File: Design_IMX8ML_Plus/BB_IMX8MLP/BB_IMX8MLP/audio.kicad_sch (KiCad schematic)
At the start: 1 part, among them U30 NAU88C22YG

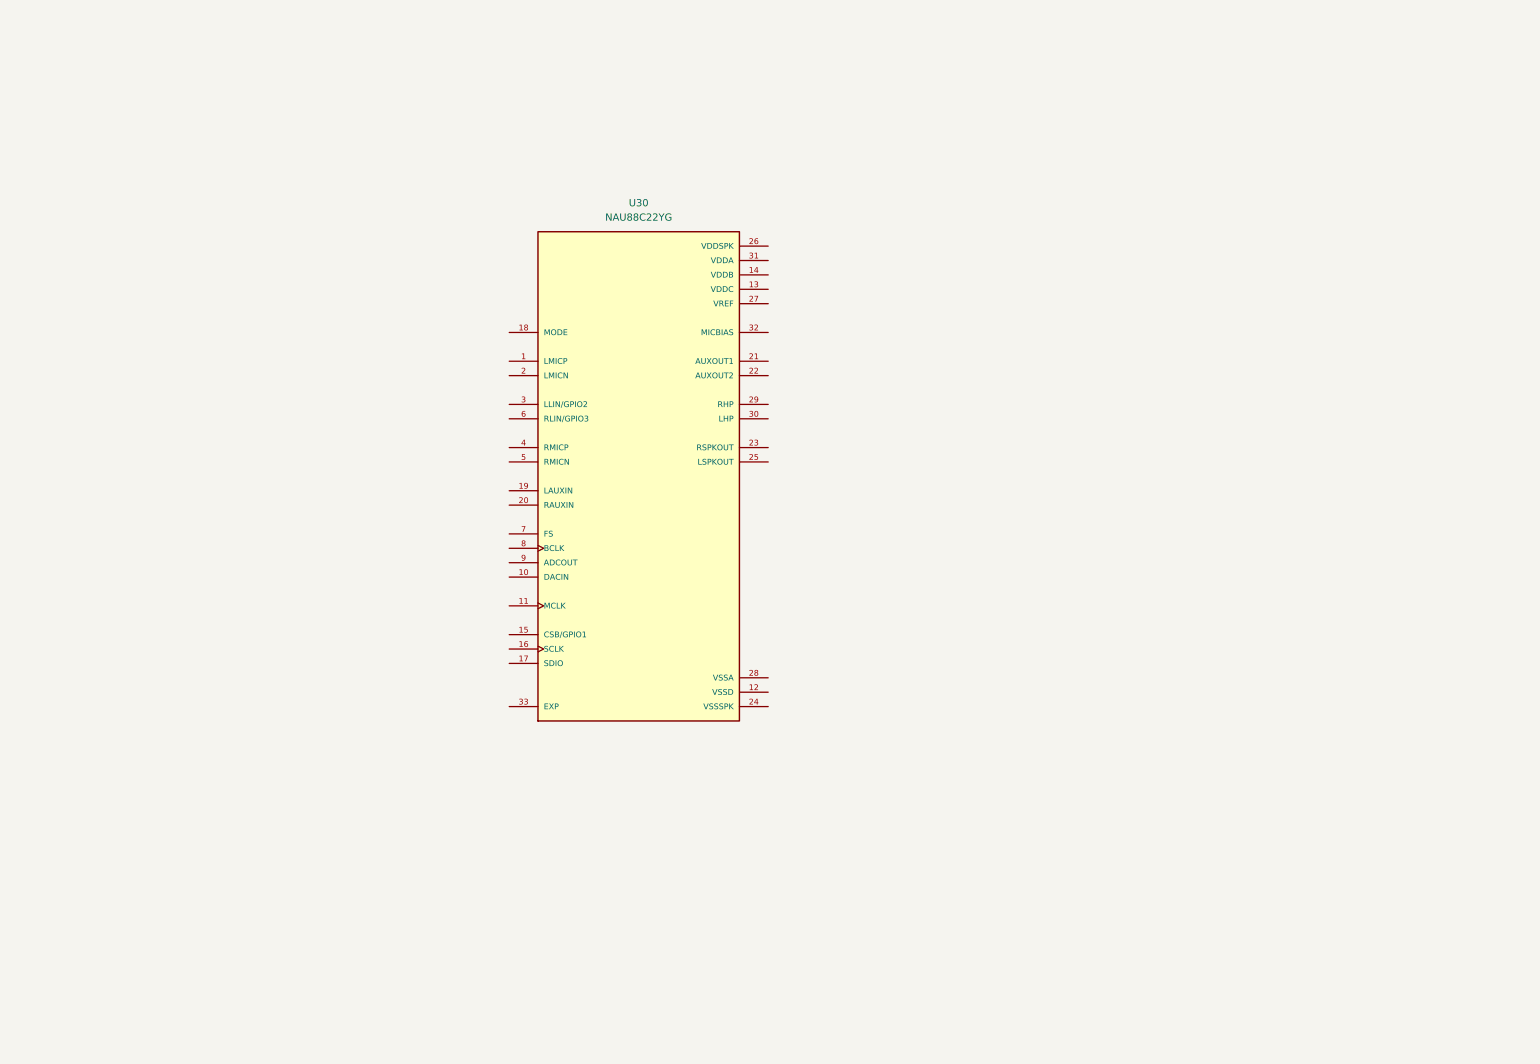
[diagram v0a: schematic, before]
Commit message: Adds audio interface
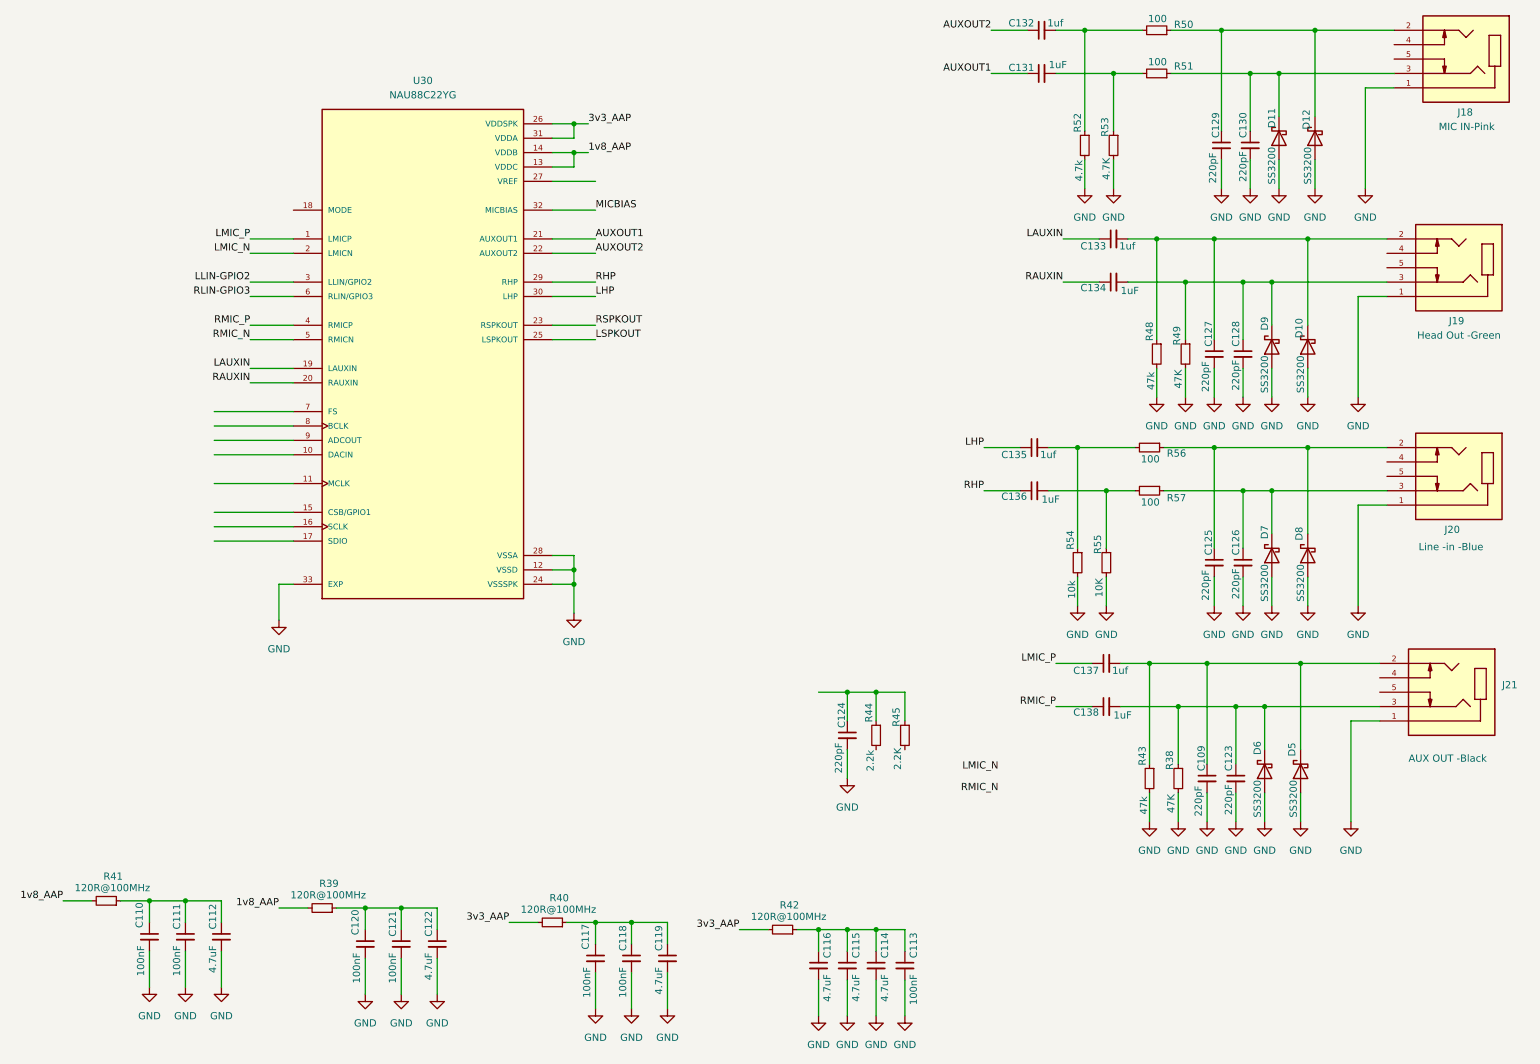
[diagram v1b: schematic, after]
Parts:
- added C109, C123, C124, C125, C126, C127, C128, C129, C130: 220pF, Capacitor_SMD:C_0402_1005Metric, symbol Device:C_Small
- added C110, C111, C113, C117, C118, C120, C121: 100nF, Capacitor_SMD:C_0402_1005Metric, symbol Device:C_Small
- added C112, C114, C115, C116, C119, C122: 4.7uF, Capacitor_SMD:C_0402_1005Metric, symbol Device:C_Small
- added C131, C134, C136, C138: 1uF, Capacitor_SMD:C_0402_1005Metric, symbol Device:C_Small
- added C132, C133, C135, C137: 1uf, Capacitor_SMD:C_0402_1005Metric, symbol Device:C_Small
- added D10, D11, D12, D5, D6, D7, D8, D9: SS3200, Diode_SMD:D_SMA, symbol Diode:SS3200
- added J18: MIC IN-Pink, _W_SBC:SJ1-3535NG-PI, symbol SJ1-3535NG-PI:SJ1-3535NG-PI
- added J19: Head Out -Green, _W_SBC:SJ1-3535NG-PI, symbol SJ1-3535NG-PI:SJ1-3535NG-PI
- added J20: Line -in -Blue, _W_SBC:SJ1-3535NG-PI, symbol SJ1-3535NG-PI:SJ1-3535NG-PI
- added J21: AUX OUT -Black, _W_SBC:SJ1-3535NG-PI, symbol SJ1-3535NG-PI:SJ1-3535NG-PI
- added R38, R49: 47K, Resistor_SMD:R_0402_1005Metric, symbol Device:R_Small
- added R39, R40, R41, R42: 120R@100MHz, Resistor_SMD:R_0402_1005Metric, symbol Device:R_Small
- added R43, R48: 47k, Resistor_SMD:R_0402_1005Metric, symbol Device:R_Small
- added R44: 2.2k, Resistor_SMD:R_0402_1005Metric, symbol Device:R_Small
- added R45: 2.2K, Resistor_SMD:R_0402_1005Metric, symbol Device:R_Small
- added R50, R51, R56, R57: 100, Resistor_SMD:R_0402_1005Metric, symbol Device:R_Small
- added R52: 4.7k, Resistor_SMD:R_0402_1005Metric, symbol Device:R_Small
- added R53: 4.7K, Resistor_SMD:R_0402_1005Metric, symbol Device:R_Small
- added R54: 10k, Resistor_SMD:R_0402_1005Metric, symbol Device:R_Small
- added R55: 10K, Resistor_SMD:R_0402_1005Metric, symbol Device:R_Small
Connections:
- net LMIC_P: now reaches U30.1 (LMICP)
- net LMIC_P: now also C137.1
- net GND: now reaches U30.12 (VSSD)
- net GND: now also U30.24 (VSSSPK), U30.28 (VSSA), U30.33 (EXP), C109.2, C110.2, C111.2, C112.2, C113.2, C114.2, C115.2, C116.2, C117.2, C118.2, C119.2, C120.2, C121.2, C122.2, C123.2, C124.2, C125.2, C126.2, C127.2, C128.2, C129.2, C130.2, D10.2 (A), D11.2 (A), D12.2 (A), D5.2 (A), D6.2 (A), D7.2 (A), D8.2 (A), D9.2 (A), J18.1, J19.1, J20.1, J21.1, R38.2, R43.2, R48.2, R49.2, R52.2, R53.2, R54.2, R55.2
- net 1v8_AAP: now reaches U30.13 (VDDC)
- net 1v8_AAP: now also U30.14 (VDDB), R39.2, R41.2
- net LAUXIN: now reaches U30.19 (LAUXIN)
- net LAUXIN: now also C133.1
- net LMIC_N: now reaches U30.2 (LMICN)
- net RAUXIN: now reaches U30.20 (RAUXIN)
- net RAUXIN: now also C134.1
- net AUXOUT1: now reaches U30.21 (AUXOUT1)
- net AUXOUT1: now also C131.1
- net AUXOUT2: now reaches U30.22 (AUXOUT2)
- net AUXOUT2: now also C132.1
- net RSPKOUT: now reaches U30.23 (RSPKOUT)
- net LSPKOUT: now reaches U30.25 (LSPKOUT)
- net 3v3_AAP: now reaches U30.26 (VDDSPK)
- net 3v3_AAP: now also U30.31 (VDDA), R40.2, R42.2
- net RHP: now reaches U30.29 (RHP)
- net RHP: now also C136.1
- net LLIN-GPIO2: now reaches U30.3 (LLIN/GPIO2)
- net LHP: now reaches U30.30 (LHP)
- net LHP: now also C135.1
- net MICBIAS: now reaches U30.32 (MICBIAS)
- net RMIC_P: now reaches U30.4 (RMICP)
- net RMIC_P: now also C138.1
- net RMIC_N: now reaches U30.5 (RMICN)
- net RLIN-GPIO3: now reaches U30.6 (RLIN/GPIO3)
- new net: C120.1, C121.1, C122.1, R39.1
- new net: C127.1, C133.2, D10.1 (K), J19.2, R48.1
- new net: C136.2, R55.1, R57.2
- new net: C135.2, R54.1, R56.2
- new net: C113.1, C114.1, C115.1, C116.1, R42.1
- new net: C126.1, D7.1 (K), J20.3, R57.1
- new net: C110.1, C111.1, C112.1, R41.1
- new net: C125.1, D8.1 (K), J20.2, R56.1
- new net: C129.1, D12.1 (K), J18.2, R50.1
- new net: C128.1, C134.2, D9.1 (K), J19.3, R49.1
- new net: C130.1, D11.1 (K), J18.3, R51.1
- new net: C109.1, C137.2, D5.1 (K), J21.2, R43.1
- new net: C131.2, R51.2, R53.1
- new net: C132.2, R50.2, R52.1
- new net: C123.1, C138.2, D6.1 (K), J21.3, R38.1
- new net: C117.1, C118.1, C119.1, R40.1
- new net: C124.1, R44.1, R45.1
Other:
- moved on the sheet: U30

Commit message: Review
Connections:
- net GND: now also U30.18 (MODE)
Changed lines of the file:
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@@
+	)
+	(junction
+		(at 62.23 114.3)
+		(diameter 0)
+		(color 0 0 0 0)
 	)
 	(junction
@@
 	(wire
 		(pts
+			(xy 62.23 48.26) (xy 64.77 48.26)
+		)
+		(stroke
+			(width 0)
+			(type default)
+		)
+	)
+	(wire
+		(pts
 			(xy 203.2 90.17) (xy 213.36 90.17)
 		)
@@
 		)
 		(stroke
+			(width 0)
+			(type default)
+		)
+	)
+	(wire
+		(pts
+			(xy 62.23 48.26) (xy 62.23 114.3)
+		)
+		(stroke

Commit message: pcb reorganization
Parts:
- removed D11, D12: SS3200, Diode_SMD:D_SMA, symbol Diode:SS3200
- added D13, D14: SS3200, Diode_SMD:D_SOD-923, symbol Diode:SS3200
- D10, D5, D6, D7, D8, D9: footprint Diode_SMD:D_SMA -> Diode_SMD:D_SOD-923
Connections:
- net GND: now also D13.2 (A), D14.2 (A)
- net at C127.1, C133.2, J19.2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: now also D14.1 (K); no longer D10.1 (K)
- net at C129.1, J18.2, R50.1: now also D10.1 (K)
- net at C128.1, C134.2, J19.3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: now also D13.1 (K); no longer D9.1 (K)
- net at C130.1, J18.3, R51.1: now also D9.1 (K)

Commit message: CPU Board actualizate
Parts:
- D10, D13, D14, D5, D6, D7, D8, D9: footprint Diode_SMD:D_SOD-923 -> Diode_SMD:D_SMA
- J18, J19, J20, J21: footprint _W_SBC:SJ1-3535NG-PI -> SJ1-3535NG-PI:CUI_SJ1-3535NG-PI
- U30: footprint _W_SBC:QFN50P500X500X80-33N -> NAU88C22YG:QFN50P500X500X80-33N
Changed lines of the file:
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@@
 			)
 		)
-		(property "Footprint" "Diode_SMD:D_SOD-923"
+		(property "Footprint" "Diode_SMD:D_SMA"
 			(at 241.935 109.22 0)
 			(effects
@@
 			)
 		)
-		(property "Footprint" "_W_SBC:QFN50P500X500X80-33N"
+		(property "Footprint" "NAU88C22YG:QFN50P500X500X80-33N"
 			(at 87.63 73.66 0)
 			(effects
@@
 			)
 		)
-		(property "Footprint" "_W_SBC:SJ1-3535NG-PI"
+		(property "Footprint" "SJ1-3535NG-PI:CUI_SJ1-3535NG-PI"
 			(at 270.51 95.25 0)
 			(effects
@@
 			)
 		)
-		(property "Footprint" "Diode_SMD:D_SOD-923"
+		(property "Footprint" "Diode_SMD:D_SMA"
 			(at 241.935 72.39 0)
 			(effects
@@
 			)
 		)
-		(property "Footprint" "Diode_SMD:D_SOD-923"
+		(property "Footprint" "Diode_SMD:D_SMA"
 			(at 247.015 147.32 0)
 			(effects
@@
 			)
 		)
-		(property "Footprint" "_W_SBC:SJ1-3535NG-PI"
+		(property "Footprint" "SJ1-3535NG-PI:CUI_SJ1-3535NG-PI"
 			(at 270.51 58.42 0)
 			(effects
@@
 			)
 		)
-		(property "Footprint" "Diode_SMD:D_SOD-923"
+		(property "Footprint" "Diode_SMD:D_SMA"
 			(at 248.285 109.22 0)
 			(effects
@@
 			)
 		)
-		(property "Footprint" "Diode_SMD:D_SOD-923"
+		(property "Footprint" "Diode_SMD:D_SMA"
 			(at 249.555 35.56 0)
 			(effects
@@
 			)
 		)
-		(property "Footprint" "Diode_SMD:D_SOD-923"
+		(property "Footprint" "Diode_SMD:D_SMA"
 			(at 243.205 35.56 0)
 			(effects
@@
 			)
 		)
-		(property "Footprint" "_W_SBC:SJ1-3535NG-PI"
+		(property "Footprint" "SJ1-3535NG-PI:CUI_SJ1-3535NG-PI"
 			(at 269.24 133.35 0)
 			(effects
@@
 			)
 		)
-		(property "Footprint" "_W_SBC:SJ1-3535NG-PI"
+		(property "Footprint" "SJ1-3535NG-PI:CUI_SJ1-3535NG-PI"
 			(at 271.78 21.59 0)
 			(effects
@@
 			)
 		)
-		(property "Footprint" "Diode_SMD:D_SOD-923"
+		(property "Footprint" "Diode_SMD:D_SMA"
 			(at 248.285 72.39 0)
 			(effects
@@
 			)
 		)
-		(property "Footprint" "Diode_SMD:D_SOD-923"
+		(property "Footprint" "Diode_SMD:D_SMA"
 			(at 240.665 147.32 0)
 			(effects

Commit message: [BB_IMX8MLP IMX8MLP] Actuallizated to 9.0 kicad version
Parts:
- removed R39, R40, R41: 120R@100MHz, Resistor_SMD:R_0402_1005Metric, symbol Device:R_Small
- added FB10, FB11, FB9: 120R@100MHz, Inductor_SMD:L_0603_1608Metric, symbol Device:FerriteBead_Small
- C109, C123, C124, C125, C126, C127, C128, C129, C130: MP (none) -> KGM05AR71H221KH; Price (none) -> 0.1
- C110, C111, C113, C117, C118, C120, C121: MP (none) -> C0402C104K4RACTU; Price (none) -> 0.1
- C112, C114, C115, C116, C119, C122: MP (none) -> CL05A475KQ5NRNC; Price (none) -> 0.1
- C131, C134, C136, C138: MP (none) -> EMK105BJ105KV-F; Price (none) -> 0.1
- D10, D9: footprint Diode_SMD:D_SMA -> Diode_SMD:D_SOD-923
- D13, D14, D5, D6, D7, D8: value SS3200 -> D5V0L1B2S9-7; footprint Diode_SMD:D_SMA -> Diode_SMD:D_SOD-923; MP (none) -> D5V0L1B2S9-7; Price (none) -> 0.75
- J18, J19, J20, J21: Price None -> 2
- R38, R49: MP (none) -> RC0402FR-0747KL; Price (none) -> 0.1
- R44, R45: MP (none) -> RC0402JR-072K2L; Price (none) -> 0.1
- R50, R51, R56, R57: MP (none) -> RC0402JR-07100RL; Price (none) -> 0.1
- R52, R53: MP (none) -> ERJ-2GEJ472X; Price (none) -> 0.1
- R54, R55: MP (none) -> RC0402JR-0710KL; Price (none) -> 0.1
- U30: Price None -> 1.5
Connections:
- net 1v8_AAP: now also FB10.1, FB9.1
- net 3v3_AAP: now also FB11.1
- net at C120.1, C121.1, C122.1: now also FB10.2
- net at C110.1, C111.1, C112.1: now also FB9.2
- net SAI5_RXFS: now reaches U30.10 (DACIN)
- net SAI1_MCLK: now reaches U30.11 (MCLK)
- net I2C1_SCL: now reaches U30.16 (SCLK)
- net I2C1_SDA: now reaches U30.17 (SDIO)
- net SAI5_RXD1: now reaches U30.7 (FS)
- net SAI5_MCLK: now reaches U30.8 (BCLK)
- net SAI1_RXD0: now reaches U30.9 (ADCOUT)
- net at C117.1, C118.1, C119.1: now also FB11.2
- no-connect marks 0 -> 1
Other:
- note added: "I2S_1_BCLK"
- note added: "I2S_1_D_IN"
- note added: "I2S_1_D_OUT"
- note added: "I2S_1_MCLK"
- note added: "I2S_1_SYNC"

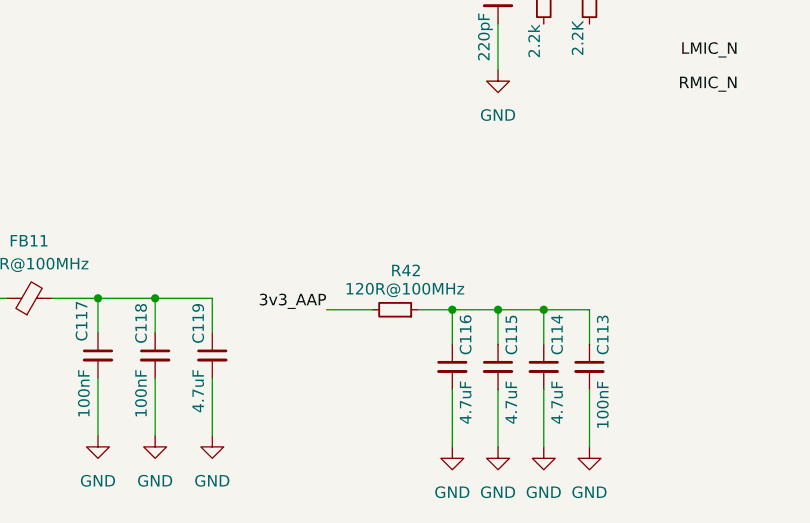
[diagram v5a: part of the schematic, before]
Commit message: [LoRa] Starting a new project
Starting a new project base on LoRa LR1121, this project use
the module LBAA0XV2GT-001 that had sub-GHz and 2.4GHz frequencies.
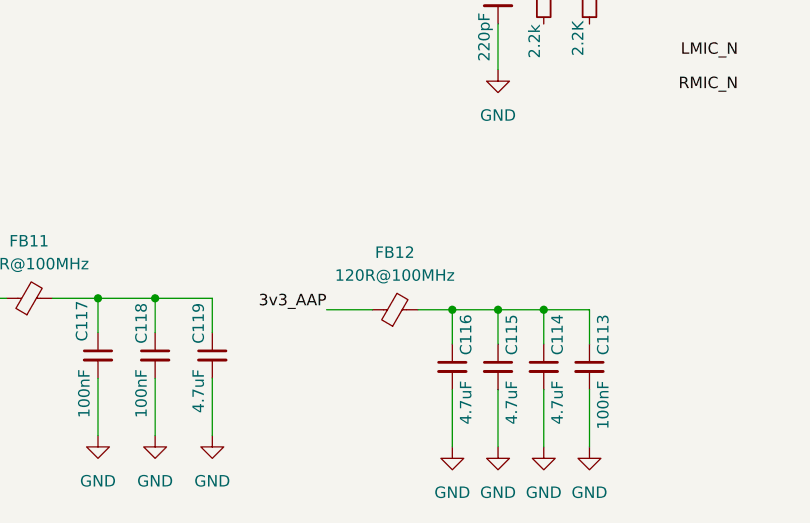
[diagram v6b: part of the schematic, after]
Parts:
- removed R42: 120R@100MHz, Resistor_SMD:R_0402_1005Metric, symbol Device:R_Small
- added FB12: 120R@100MHz, Inductor_SMD:L_0603_1608Metric, symbol Device:FerriteBead_Small
- D10, D9: MP (none) -> SS3200; Price (none) -> 0.5
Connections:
- net 3v3_AAP: now also FB12.1
- net at C113.1, C114.1, C115.1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: now also FB12.2
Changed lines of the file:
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@@
 	)
 	(symbol
+		(lib_id "Device:FerriteBead_Small")
+		(at 151.13 175.26 90)
+		(unit 1)
+		(exclude_from_sim no)
+		(in_bom yes)
+		(on_board yes)
+		(dnp no)
+		(fields_autoplaced yes)
+		(property "Reference" "FB12"
+			(at 151.0919 168.91 90)
+			(effects
+				(font
+					(size 1.27 1.27)
+				)
+			)
+		)
+		(property "Value" "120R@100MHz"
+			(at 151.0919 171.45 90)
+			(effects
+				(font
+					(size 1.27 1.27)
+				)
+			)
+		)
+		(property "Footprint" "Inductor_SMD:L_0603_1608Metric"
+			(at 153.6318 172.72 0)
+			(effects
+				(font
+					(size 1.27 1.27)
+				)
+				(justify left)
+				(hide yes)
+			)
+		)
+		(property "Datasheet" "~"
+			(at 151.13 175.26 0)
+			(effects
+				(font
+					(size 1.27 1.27)
+				)
+				(hide yes)
+			)
+		)
+		(property "Description" "Ferrite bead, small symbol"
+			(at 151.13 175.26 0)
+			(effects
+				(font
+					(size 1.27 1.27)
+				)
+				(hide yes)
+			)
+		)
+		(property "MP" "MPZ1608S121ATAH0"
+			(at 151.13 175.26 0)
+			(effects
+				(font
+					(size 1.27 1.27)
+				)
+				(hide yes)
+			)
+		)
+		(property "Price" "0.1"
+			(at 151.13 175.26 0)
+			(effects
+				(font
+					(size 1.27 1.27)
+				)
+				(hide yes)
+			)
+		)
+		(pin "2"
+		)
+		(pin "1"
+		)
+		(instances
+			(project "BB_IMX8MLP"
+				(path "/cd2fb234-91e5-476f-84ed-38419b628dc6/6b35cf2a-ff76-4c8b-8fd9-fa59a1552b9f"
+					(reference "FB12")
+					(unit 1)
+				)
+			)
+		)
+	)
+	(symbol
 		(lib_id "Device:R_Small")
 		(at 203.2 110.49 0)
@@
 			)
 		)
+		(property "MP" "SS3200"
+			(at 245.11 35.56 0)
+			(effects
+				(font
+					(size 1.27 1.27)
+				)
+				(hide yes)
+			)
+		)
+		(property "Price" "0.5"
+			(at 245.11 35.56 0)
+			(effects
+				(font
+					(size 1.27 1.27)
+				)
+				(hide yes)
+			)
+		)
 		(pin "2"
 		)
@@
 			)
 		)
+		(property "MP" "SS3200"
+			(at 238.76 35.56 0)
+			(effects
+				(font
+					(size 1.27 1.27)
+				)
+				(hide yes)
+			)
+		)
+		(property "Price" "0.5"
+			(at 238.76 35.56 0)
+			(effects
+				(font
+					(size 1.27 1.27)
+				)
+				(hide yes)
+			)
+		)
 		(pin "2"
 		)
@@
 					(unit 1)
 				)
-			)
-		)
-	)
-	(symbol
-		(lib_id "Device:R_Small")
-		(at 151.13 175.26 270)
-		(mirror x)
-		(unit 1)
-		(exclude_from_sim no)
-		(in_bom yes)
-		(on_board yes)
-		(dnp no)
-		(property "Reference" "R42"
-			(at 150.622 170.942 90)
-			(effects
-				(font
-					(size 1.27 1.27)
-				)
-				(justify left)
-			)
-		)
-		(property "Value" "120R@100MHz"
-			(at 145.542 172.974 90)
-			(effects
-				(font
-					(size 1.27 1.27)
-				)
-				(justify left)
-			)
-		)
-		(property "Footprint" "Resistor_SMD:R_0402_1005Metric"
-			(at 151.13 175.26 0)
-			(effects
-				(font
-					(size 1.27 1.27)
-				)
-				(hide yes)
-			)
-		)
-		(property "Datasheet" "~"
-			(at 151.13 175.26 0)
-			(effects
-				(font
-					(size 1.27 1.27)
-				)
-				(hide yes)
-			)
-		)
-		(property "Description" "Resistor, small symbol"
-			(at 151.13 175.26 0)
-			(effects
-				(font
-					(size 1.27 1.27)
-				)
-				(hide yes)
-			)
-		)
-		(property "Sim.Device" ""
-			(at 151.13 175.26 90)
-			(effects
-				(font
-					(size 1.27 1.27)
-				)
-				(hide yes)
-			)
-		)
-		(property "Sim.Pins" ""
-			(at 151.13 175.26 90)
-			(effects
-				(font
-					(size 1.27 1.27)
-				)
-				(hide yes)
-			)
-		)
-		(pin "1"
-		)
-		(pin "2"
-		)
-		(instances
-			(project "BB_IMX8MLP"
-				(path "/cd2fb234-91e5-476f-84ed-38419b628dc6/6b35cf2a-ff76-4c8b-8fd9-fa59a1552b9f"
-					(reference "R42")
-					(unit 1)
-				)
